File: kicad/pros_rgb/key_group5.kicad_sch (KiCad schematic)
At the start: 17 parts

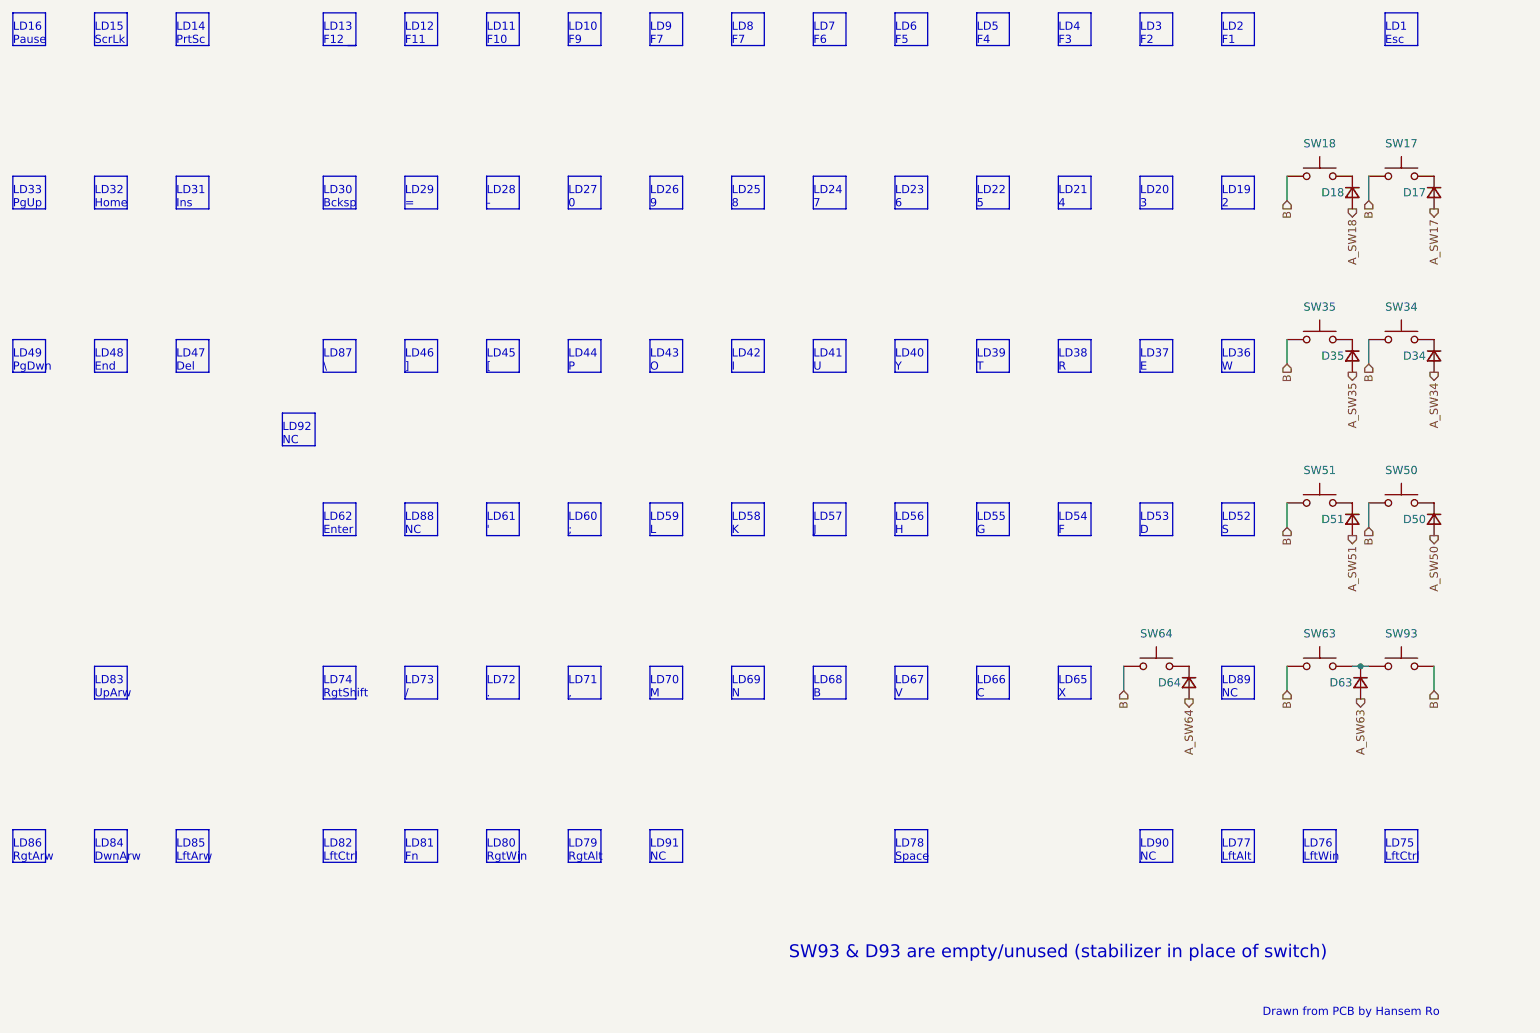
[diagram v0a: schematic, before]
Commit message: kicad/pros_rgb: update key groupings
These new groupings are based off ordering in firmware:
https://github.com/hansemro/pok3r_re_firmware/blob/4b68aa4baf7d28dc8dbf8eebcb1fdb59e7bcd629/disassemble/cmprosrgb/v122/cmprosrgb_v122.txt#L14599-L14629
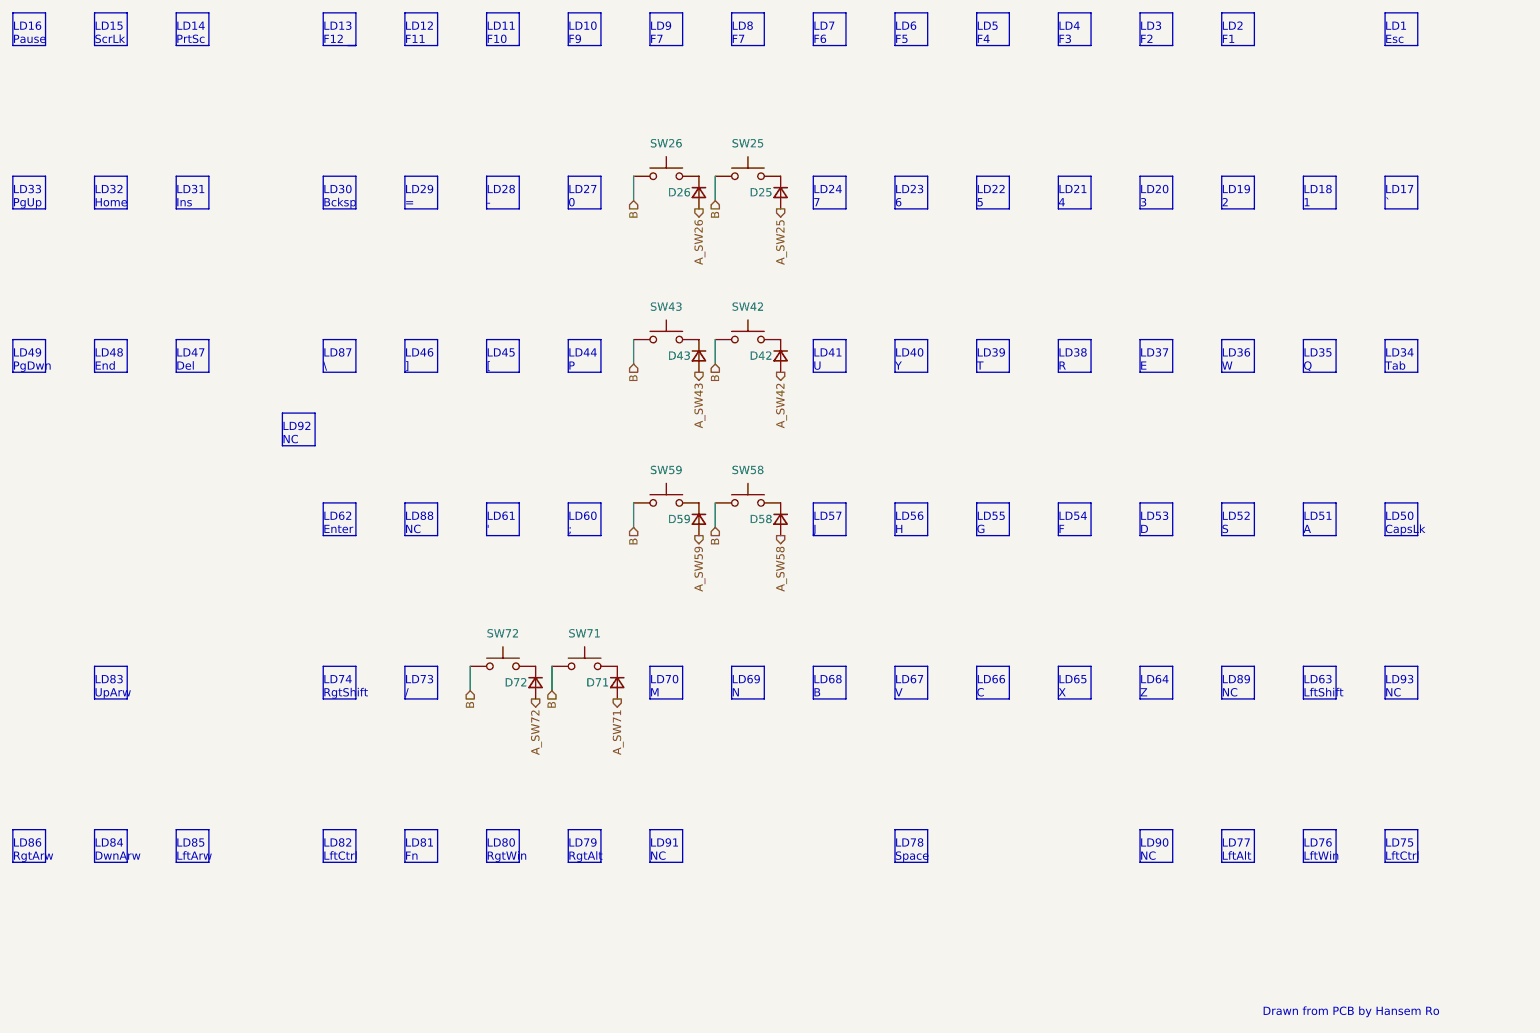
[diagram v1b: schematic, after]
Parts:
- removed D17, D18, D34, D35, D50, D51, D63, D64: ~, symbol Device:D_Small
- removed SW17, SW18, SW34, SW35, SW50, SW51, SW63, SW64, SW93: ~, symbol Switch:SW_Push
- added D25, D26, D42, D43, D58, D59, D71, D72: (no value), symbol Device:D_Small
- added SW25, SW26, SW42, SW43, SW58, SW59, SW71, SW72: (no value), symbol Switch:SW_Push
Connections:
- net B: now also SW25.1, SW26.1, SW42.1, SW43.1, SW58.1, SW59.1, SW71.1, SW72.1
- new net: D42.1 (K), SW42.2
- new net: D25.1 (K), SW25.2
- new net: D43.1 (K), SW43.2
- new net: D72.1 (K), SW72.2
- new net: D59.1 (K), SW59.2
- new net: D71.1 (K), SW71.2
- new net: D26.1 (K), SW26.2
- new net: D58.1 (K), SW58.2
- new net A_SW25: D25.2 (A)
- new net A_SW26: D26.2 (A)
- new net A_SW42: D42.2 (A)
- new net A_SW43: D43.2 (A)
- new net A_SW58: D58.2 (A)
- new net A_SW59: D59.2 (A)
- new net A_SW71: D71.2 (A)
- new net A_SW72: D72.2 (A)
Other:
- note added: "LD17 `"
- note added: "LD18 1"
- note added: "LD34 Tab"
- note added: "LD35 Q"
- note added: "LD50 CapsLk"
- note added: "LD51 A"
- note added: "LD63 LftShift"
- note added: "LD64 Z"
- note added: "LD93 NC"
- note removed: "LD25 8"
- note removed: "LD26 9"
- note removed: "LD42 I"
- note removed: "LD43 O"
- note removed: "LD58 K"
- note removed: "LD59 L"
- note removed: "LD71 ,"
- note removed: "LD72 ."
- note removed: "SW93 & D93 are empty/unused (stabilizer in place of switch)"

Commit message: kicad/pros_rgb: mark as Rev. B
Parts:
- D25, D26, D42, D43, D58, D59, D71, D72, SW25, SW26, SW42, SW43, SW58, SW59, SW71, SW72: value (none) -> ~
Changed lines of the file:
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@@
     (in_bom yes) (on_board yes)
     (property "Reference" "SW42" (id 0) (at 172.72 69.85 0))
-    (property "Value" "" (id 1) (at 172.72 69.85 0))
+    (property "Value" "~" (id 1) (at 172.72 69.85 0))
     (property "Footprint" "" (id 2) (at 172.72 69.85 0)
       (effects (font (size 1.27 1.27)) hide)
@@
     (in_bom yes) (on_board yes)
     (property "Reference" "SW25" (id 0) (at 172.72 44.45 0))
-    (property "Value" "" (id 1) (at 172.72 44.45 0))
+    (property "Value" "~" (id 1) (at 172.72 44.45 0))
     (property "Footprint" "" (id 2) (at 172.72 44.45 0)
       (effects (font (size 1.27 1.27)) hide)
@@
       (effects (font (size 1.27 1.27)) (justify right))
     )
-    (property "Value" "" (id 1) (at 167.64 78.7399 90)
+    (property "Value" "~" (id 1) (at 167.64 78.7399 90)
       (effects (font (size 1.27 1.27)) (justify left))
     )
@@
       (effects (font (size 1.27 1.27)) (justify right))
     )
-    (property "Value" "" (id 1) (at 142.24 129.5399 90)
+    (property "Value" "~" (id 1) (at 142.24 129.5399 90)
       (effects (font (size 1.27 1.27)) (justify left))
     )
@@
       (effects (font (size 1.27 1.27)) (justify right))
     )
-    (property "Value" "" (id 1) (at 180.34 53.3399 90)
+    (property "Value" "~" (id 1) (at 180.34 53.3399 90)
       (effects (font (size 1.27 1.27)) (justify left))
     )
@@
       (effects (font (size 1.27 1.27)) (justify right))
     )
-    (property "Value" "" (id 1) (at 167.64 104.1399 90)
+    (property "Value" "~" (id 1) (at 167.64 104.1399 90)
       (effects (font (size 1.27 1.27)) (justify left))
     )
@@
     (in_bom yes) (on_board yes)
     (property "Reference" "SW43" (id 0) (at 160.02 69.85 0))
-    (property "Value" "" (id 1) (at 160.02 69.85 0))
+    (property "Value" "~" (id 1) (at 160.02 69.85 0))
     (property "Footprint" "" (id 2) (at 160.02 69.85 0)
       (effects (font (size 1.27 1.27)) hide)
@@
     (in_bom yes) (on_board yes)
     (property "Reference" "SW71" (id 0) (at 147.32 120.65 0))
-    (property "Value" "" (id 1) (at 147.32 120.65 0))
+    (property "Value" "~" (id 1) (at 147.32 120.65 0))
     (property "Footprint" "" (id 2) (at 147.32 120.65 0)
       (effects (font (size 1.27 1.27)) hide)
@@
       (effects (font (size 1.27 1.27)) (justify right))
     )
-    (property "Value" "" (id 1) (at 180.34 78.7399 90)
+    (property "Value" "~" (id 1) (at 180.34 78.7399 90)
       (effects (font (size 1.27 1.27)) (justify left))
     )
@@
       (effects (font (size 1.27 1.27)) (justify right))
     )
-    (property "Value" "" (id 1) (at 154.94 129.5399 90)
+    (property "Value" "~" (id 1) (at 154.94 129.5399 90)
       (effects (font (size 1.27 1.27)) (justify left))
     )
@@
     (in_bom yes) (on_board yes)
     (property "Reference" "SW72" (id 0) (at 134.62 120.65 0))
-    (property "Value" "" (id 1) (at 134.62 120.65 0))
+    (property "Value" "~" (id 1) (at 134.62 120.65 0))
     (property "Footprint" "" (id 2) (at 134.62 120.65 0)
       (effects (font (size 1.27 1.27)) hide)
@@
       (effects (font (size 1.27 1.27)) (justify right))
     )
-    (property "Value" "" (id 1) (at 167.64 53.3399 90)
+    (property "Value" "~" (id 1) (at 167.64 53.3399 90)
       (effects (font (size 1.27 1.27)) (justify left))
     )
@@
     (in_bom yes) (on_board yes)
     (property "Reference" "SW26" (id 0) (at 160.02 44.45 0))
-    (property "Value" "" (id 1) (at 160.02 44.45 0))
+    (property "Value" "~" (id 1) (at 160.02 44.45 0))
     (property "Footprint" "" (id 2) (at 160.02 44.45 0)
       (effects (font (size 1.27 1.27)) hide)
@@
       (effects (font (size 1.27 1.27)) (justify right))
     )
-    (property "Value" "" (id 1) (at 180.34 104.1399 90)
+    (property "Value" "~" (id 1) (at 180.34 104.1399 90)
       (effects (font (size 1.27 1.27)) (justify left))
     )
@@
     (in_bom yes) (on_board yes)
     (property "Reference" "SW58" (id 0) (at 172.72 95.25 0))
-    (property "Value" "" (id 1) (at 172.72 95.25 0))
+    (property "Value" "~" (id 1) (at 172.72 95.25 0))
     (property "Footprint" "" (id 2) (at 172.72 95.25 0)
       (effects (font (size 1.27 1.27)) hide)
@@
     (in_bom yes) (on_board yes)
     (property "Reference" "SW59" (id 0) (at 160.02 95.25 0))
-    (property "Value" "" (id 1) (at 160.02 95.25 0))
+    (property "Value" "~" (id 1) (at 160.02 95.25 0))
     (property "Footprint" "" (id 2) (at 160.02 95.25 0)
       (effects (font (size 1.27 1.27)) hide)

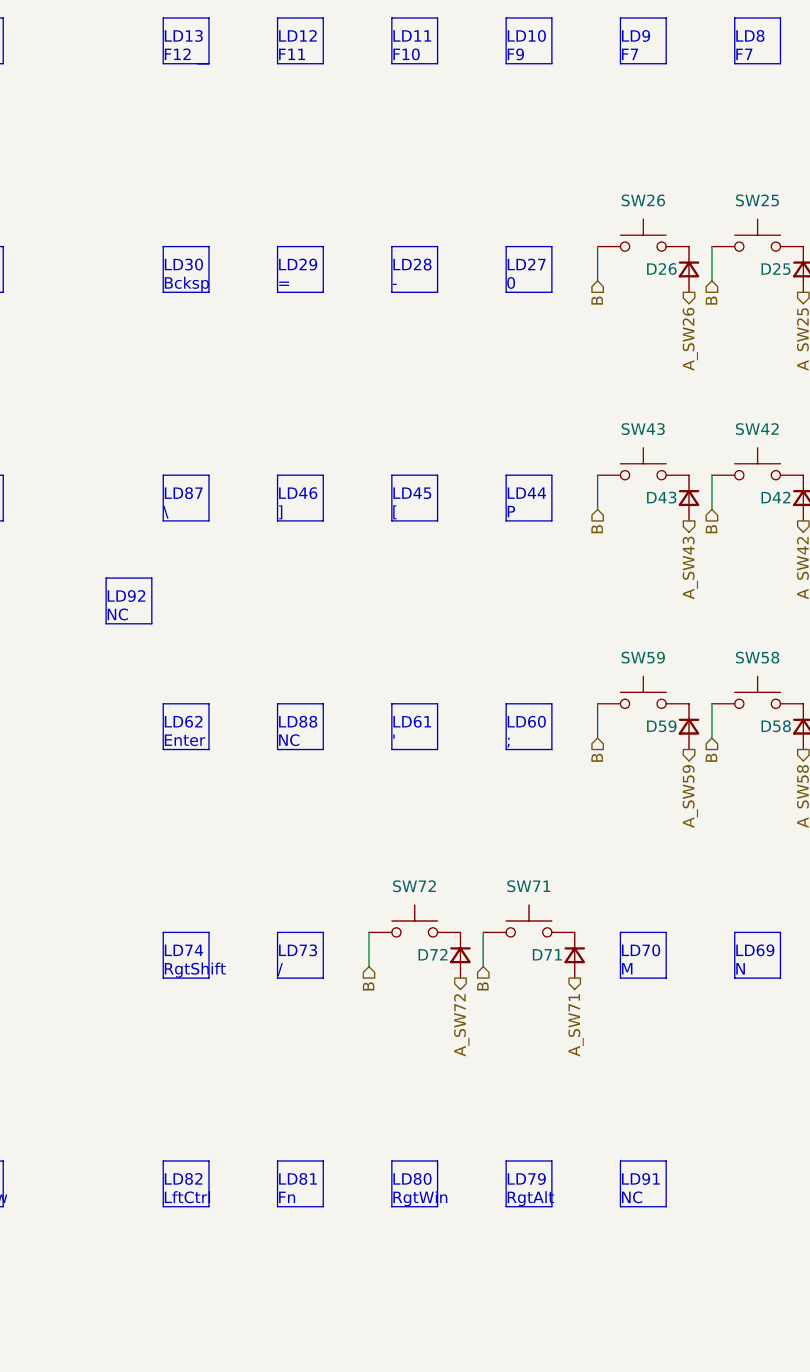
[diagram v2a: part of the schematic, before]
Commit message: kicad/pros_rgb: fix typos
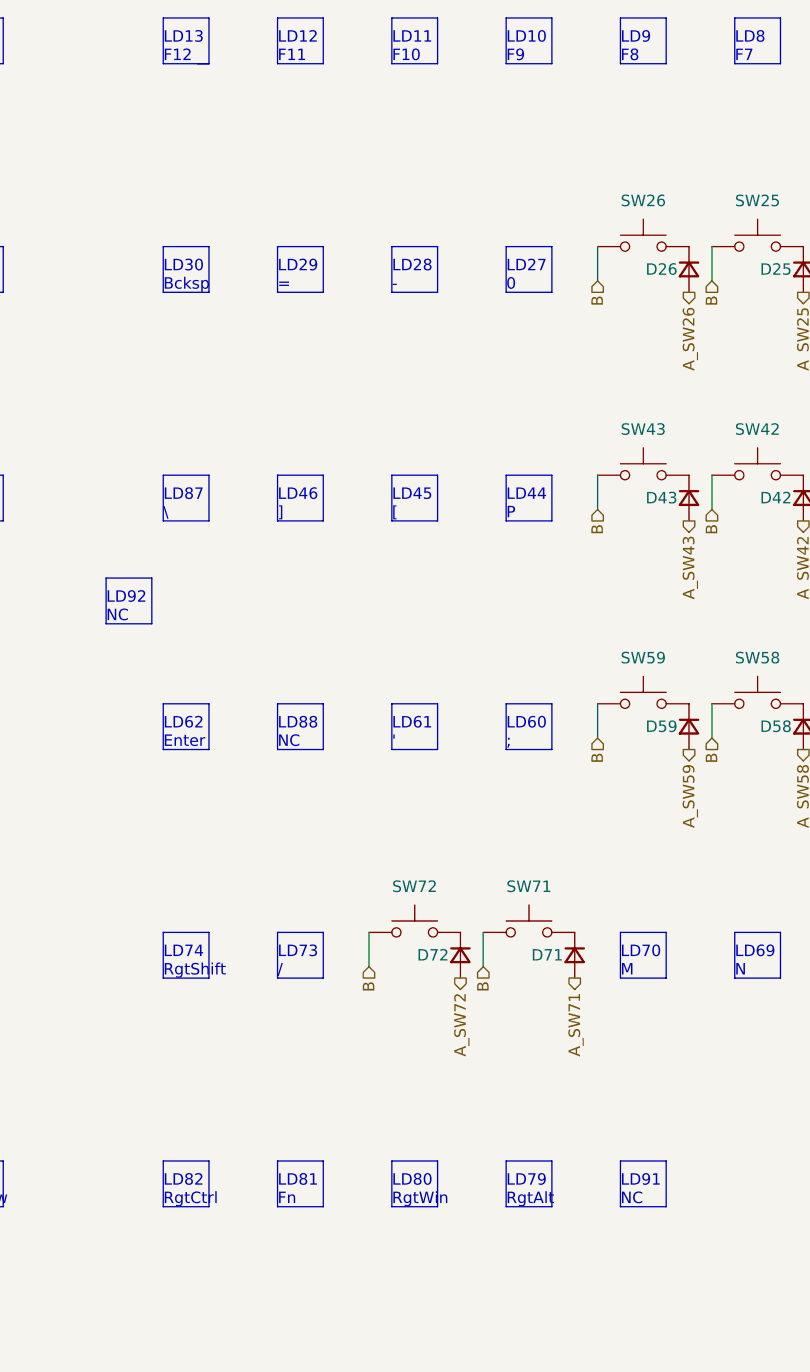
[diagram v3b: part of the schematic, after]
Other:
- note added: "LD82 RgtCtrl"
- note added: "LD9 F8"
- note removed: "LD82 LftCtrl"
- note removed: "LD9 F7"
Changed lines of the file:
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@@
     (effects (font (size 1.27 1.27)) (justify left bottom))
   )
-  (text "LD9\nF7" (at 157.48 29.21 0)
+  (text "LD9\nF8" (at 157.48 29.21 0)
     (effects (font (size 1.27 1.27)) (justify left bottom))
   )
@@
     (effects (font (size 1.27 1.27)) (justify left bottom))
   )
-  (text "LD82\nLftCtrl" (at 106.68 156.21 0)
+  (text "LD82\nRgtCtrl" (at 106.68 156.21 0)
     (effects (font (size 1.27 1.27)) (justify left bottom))
   )
